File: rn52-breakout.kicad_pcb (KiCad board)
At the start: 2 copper layers, 15 parts, among them K1 CONN_3, P1 CONN_4, P2 CONN_2, P3 CONN_2, P4 CONN_2, U1 LM317T, U2 RN52

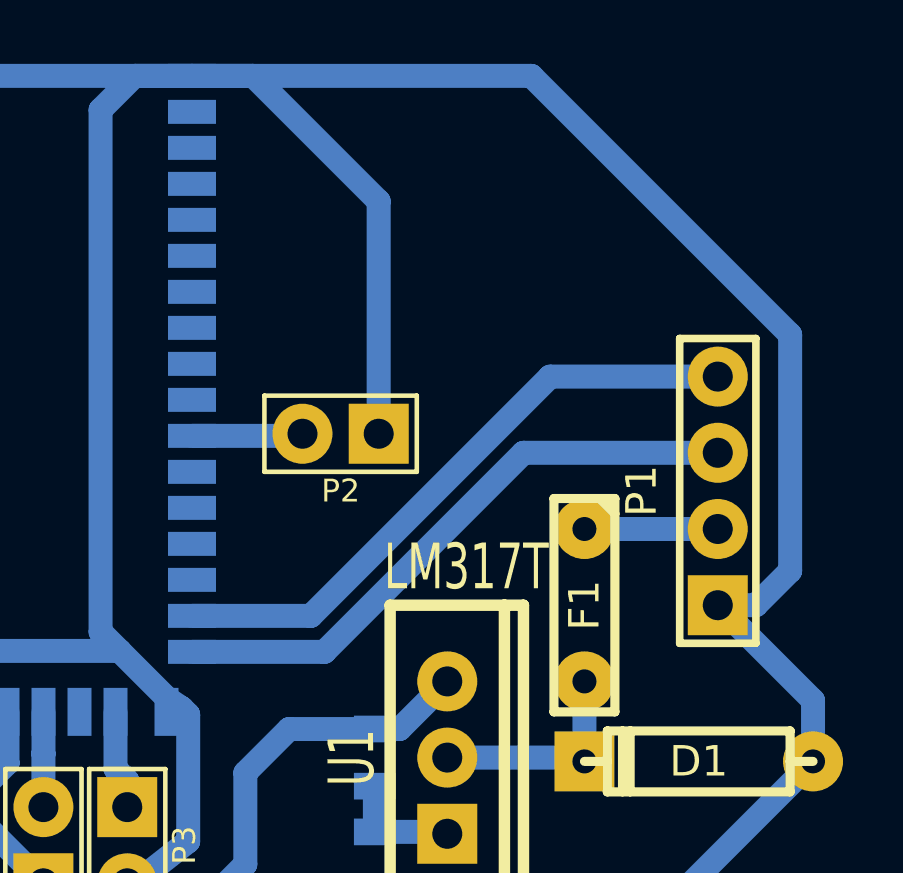
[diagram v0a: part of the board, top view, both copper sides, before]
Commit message: Pre-production version, still need a footprint for audio connector
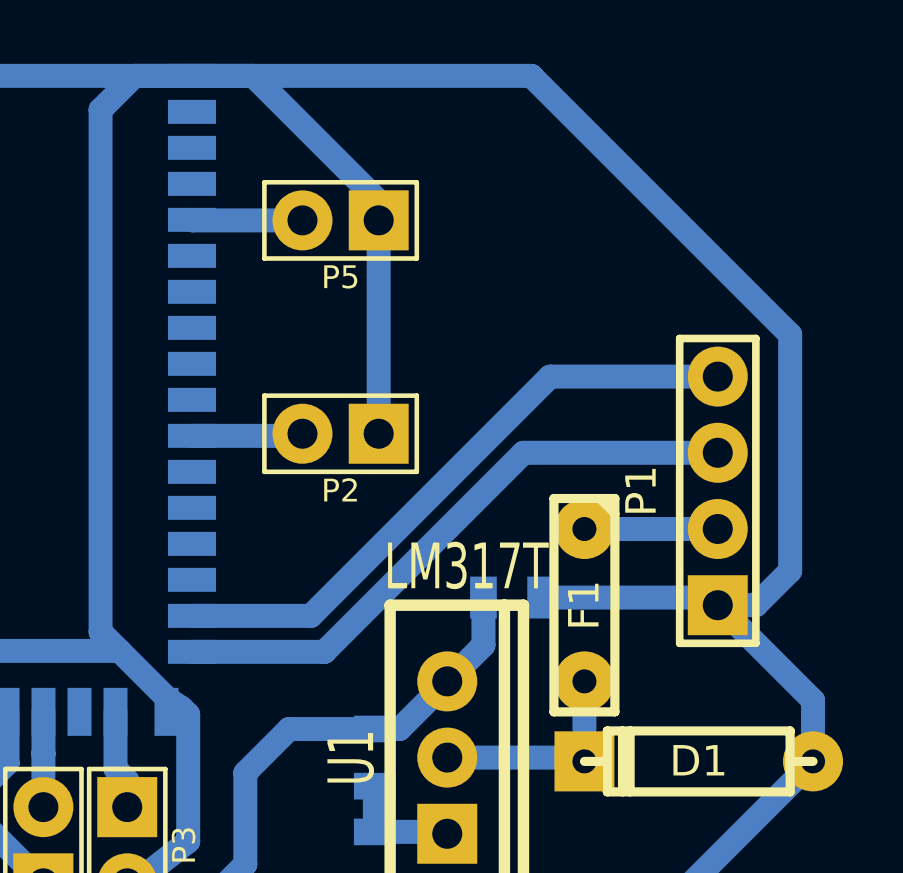
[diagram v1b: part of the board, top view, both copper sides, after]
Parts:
- added C1: 1uF, SM0805, B.Cu at (70.2, 35.8)
- added P5: FACTORY, PIN_ARRAY_2X1, F.Cu at (64.5, 23.2)
- P1: value CONN_4 -> UART
- P2: value CONN_2 -> MODE_SET
- P3: value CONN_2 -> BAUD_SET
- P4: value CONN_2 -> PWREN
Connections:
- U2 pad 5: (no net) -> N-0000011
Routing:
- net GND: track 129.5 -> 135.5 mm
- net N-0000011: track 0.00 -> 3.69 mm
- net +3.3V: track 49.6 -> 52.9 mm

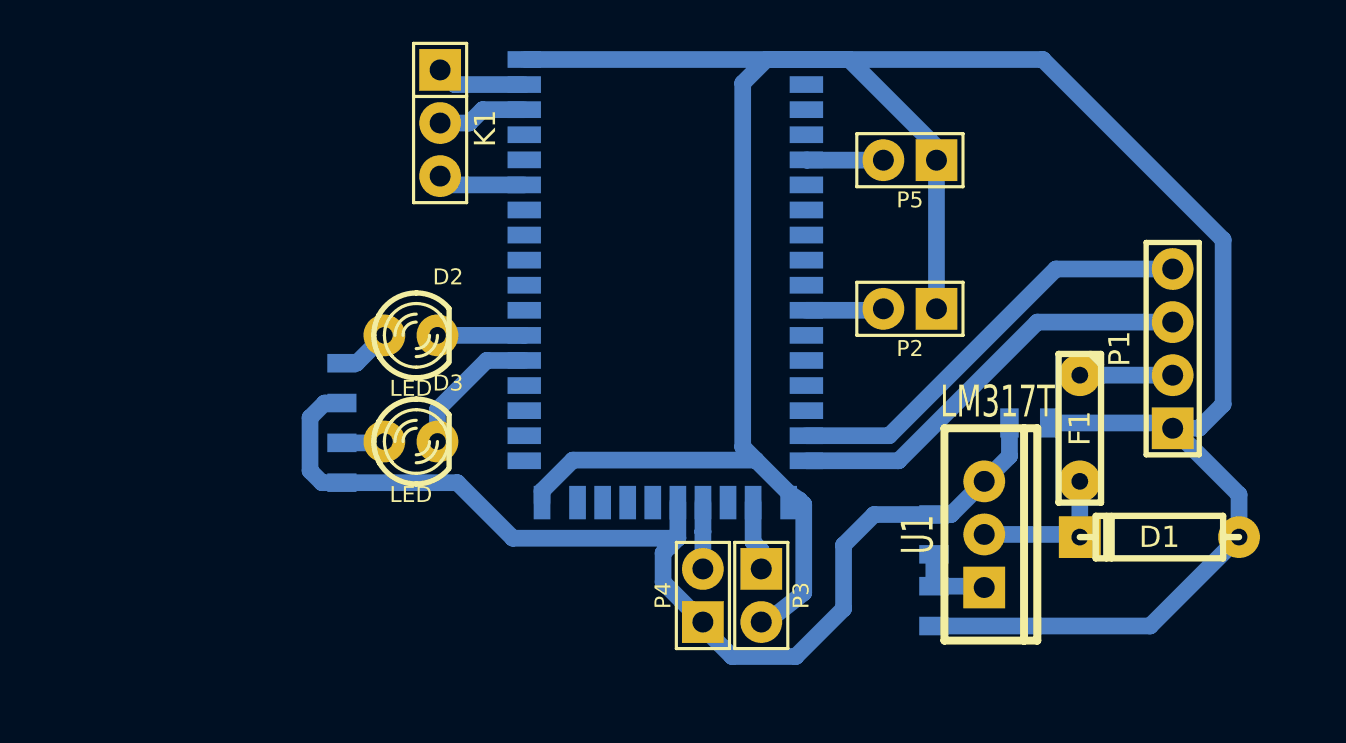
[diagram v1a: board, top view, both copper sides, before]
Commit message: Added 3.5mm jack connector
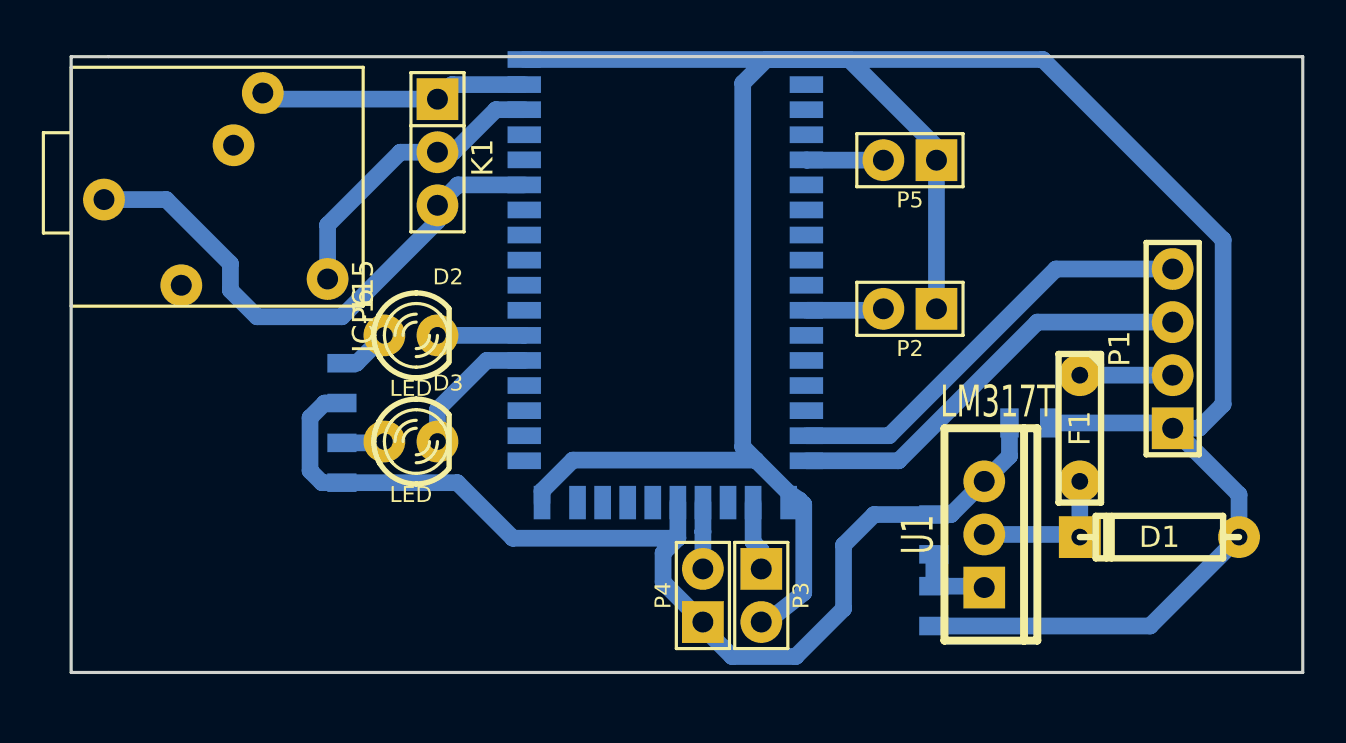
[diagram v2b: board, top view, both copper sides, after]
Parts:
- added P6: JC-115, JC-115, F.Cu at (38.4, 30.2)
- moved K1 1.40 mm to (41.9, 22.9)
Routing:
- net N-0000010: track 4.20 -> 26.2 mm
- net N-0000011: track 4.29 -> 14.3 mm
- net N-0000012: track 4.32 -> 12.9 mm
- added copper zone on B.Cu, net GND
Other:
- board outline added: 58.9 x 29.5 mm

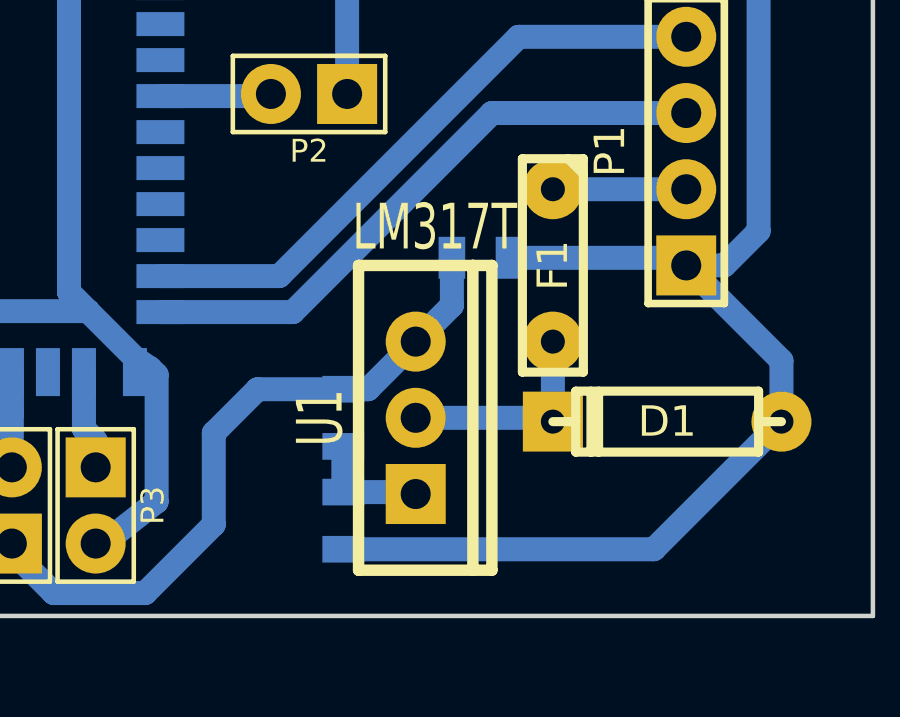
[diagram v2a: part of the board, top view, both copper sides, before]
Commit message: Fixed incorrect pinout for lin. regul., added some vanity pictures
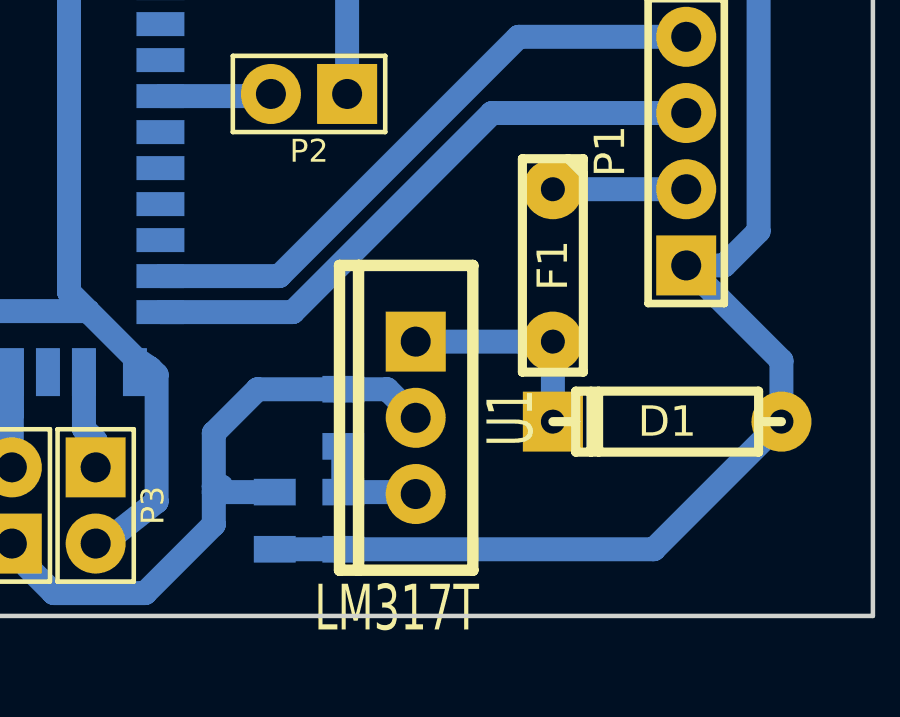
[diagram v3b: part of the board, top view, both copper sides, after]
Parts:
- moved C1 11.1 mm to (63.4, 44.6), turned to 270 degrees
- turned U1 to 180 degrees
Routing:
- net GND: track 135.5 -> 131.7 mm
- net +3.3V: track 52.9 -> 52.0 mm
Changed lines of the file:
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@@
     (thickness 1.6)
     (drawings 8)
-    (tracks 103)
+    (tracks 104)
     (zones 0)
     (modules 18)
@@
   )
   (module TO220_VERT (layer F.Cu)
-    (at 68.072 41.148)
+    (at 68.072 41.148 180)
     (descr "Regulateur TO220 serie LM78xx")
     (tags "TR TO220")
-    (fp_text reference U1 (at -3.175 0 90) (layer F.SilkS)
+    (fp_text reference U1 (at -3.175 0 270) (layer F.SilkS)
       (effects (font (size 1.524 1.016) (thickness 0.2032)))
     )
-    (fp_text value LM317T (at 0.635 -6.35) (layer F.SilkS)
+    (fp_text value LM317T (at 0.635 -6.35 180) (layer F.SilkS)
       (effects (font (size 1.524 1.016) (thickness 0.2032)))
     )
@@
     (fp_line (start 1.905 5.08) (end -1.905 5.08) (layer F.SilkS) (width 0.381))
     (fp_line (start -1.905 5.08) (end -1.905 -5.08) (layer F.SilkS) (width 0.381))
-    (pad 2 thru_hole circle (at 0 -2.54) (size 2 2) (drill 1)
+    (pad 1 thru_hole circle (at 0 -2.54 180) (size 2 2) (drill 1)
+      (layers *.Cu *.Mask F.SilkS)
+      (net 15 N-000005)
+    )
+    (pad 2 thru_hole circle (at 0 0 180) (size 2 2) (drill 1)
       (layers *.Cu *.Mask F.SilkS)
       (net 1 +3.3V)
     )
-    (pad 3 thru_hole circle (at 0 0) (size 2 2) (drill 1)
+    (pad 3 thru_hole rect (at 0 2.54 180) (size 2 2) (drill 1)
       (layers *.Cu *.Mask F.SilkS)
       (net 18 N-000006)
     )
-    (pad 1 thru_hole rect (at 0 2.54) (size 2 2) (drill 1)
-      (layers *.Cu *.Mask F.SilkS)
-      (net 15 N-000005)
-    )
   )
   (module SM0805 (layer B.Cu)
-    (at 70.231 35.814)
+    (at 63.373 44.577 270)
     (attr smd)
-    (fp_text reference C1 (at 0 0.3175) (layer B.SilkS)
+    (fp_text reference C1 (at 0 0.3175 270) (layer B.SilkS)
       (effects (font (size 0.50038 0.50038) (thickness 0.10922)) (justify mirror))
     )
-    (fp_text value 1uF (at 0 -0.381) (layer B.SilkS)
+    (fp_text value 1uF (at 0 -0.381 270) (layer B.SilkS)
       (effects (font (size 0.50038 0.50038) (thickness 0.10922)) (justify mirror))
     )
@@
     (fp_line (start 1.524 0.762) (end 1.524 -0.762) (layer B.SilkS) (width 0.09906))
     (fp_line (start 1.524 -0.762) (end 0.508 -0.762) (layer B.SilkS) (width 0.09906))
-    (pad 1 smd rect (at -0.9525 0) (size 0.889 1.397)
+    (pad 1 smd rect (at -0.9525 0 270) (size 0.889 1.397)
       (layers B.Cu B.Paste B.Mask)
       (net 1 +3.3V)
     )
-    (pad 2 smd rect (at 0.9525 0) (size 0.889 1.397)
+    (pad 2 smd rect (at 0.9525 0 270) (size 0.889 1.397)
       (layers B.Cu B.Paste B.Mask)
       (net 3 GND)
@@
   (gr_line (start 26.162 47.752) (end 83.312 47.752) (angle 90) (layer Edge.Cuts) (width 0.15))
   (gr_line (start 83.312 18.288) (end 83.312 47.752) (angle 90) (layer Edge.Cuts) (width 0.15))
-  (segment (start 69.2785 35.814) (end 69.2785 37.4015) (width 0.8) (layer B.Cu) (net 1))
-  (segment (start 69.2785 37.4015) (end 68.072 38.608) (width 0.8) (layer B.Cu) (net 1))
+  (segment (start 63.373 43.6245) (end 61.341 43.6245) (width 0.8) (layer B.Cu) (net 1))
+  (segment (start 61.595 43.434) (end 61.341 43.434) (width 0.8) (layer B.Cu) (net 1))
+  (segment (start 61.5315 43.434) (end 61.595 43.434) (width 0.8) (layer B.Cu) (net 1))
+  (segment (start 61.341 43.6245) (end 61.5315 43.434) (width 0.8) (layer B.Cu) (net 1))
+  (segment (start 65.659 40.1955) (end 67.1195 40.1955) (width 0.8) (layer B.Cu) (net 1))
+  (segment (start 67.1195 40.1955) (end 68.072 41.148) (width 0.8) (layer B.Cu) (net 1))
   (segment (start 54.61 45.339) (end 54.61 45.593) (width 0.8) (layer B.Cu) (net 1))
   (segment (start 62.8015 40.1955) (end 65.659 40.1955) (width 0.8) (layer B.Cu) (net 1))
   (segment (start 61.341 41.656) (end 62.8015 40.1955) (width 0.8) (layer B.Cu) (net 1))
-  (segment (start 61.341 44.704) (end 61.341 41.656) (width 0.8) (layer B.Cu) (net 1))
+  (segment (start 61.341 44.704) (end 61.341 43.434) (width 0.8) (layer B.Cu) (net 1))
+  (segment (start 61.341 43.434) (end 61.341 41.656) (width 0.8) (layer B.Cu) (net 1))
   (segment (start 59.055 46.99) (end 61.341 44.704) (width 0.8) (layer B.Cu) (net 1))
   (segment (start 56.007 46.99) (end 59.055 46.99) (width 0.8) (layer B.Cu) (net 1))
@@
   (segment (start 45.52 41.329) (end 53.413 41.329) (width 0.8) (layer B.Cu) (net 1))
   (segment (start 42.8625 38.6715) (end 45.52 41.329) (width 0.8) (layer B.Cu) (net 1))
-  (segment (start 65.659 40.1955) (end 66.4845 40.1955) (width 0.8) (layer B.Cu) (net 1))
-  (segment (start 66.4845 40.1955) (end 68.072 38.608) (width 0.8) (layer B.Cu) (net 1))
   (segment (start 53.413 39.624) (end 53.413 41.329) (width 0.8) (layer B.Cu) (net 1))
   (segment (start 53.413 41.329) (end 52.705 42.037) (width 0.8) (layer B.Cu) (net 1))
@@
   (segment (start 36.5125 34.8615) (end 35.814 35.56) (width 0.8) (layer B.Cu) (net 1))
   (segment (start 77.089 33.528) (end 72.644 33.528) (width 0.8) (layer B.Cu) (net 2))
-  (segment (start 71.1835 35.814) (end 76.835 35.814) (width 0.8) (layer B.Cu) (net 3))
-  (segment (start 76.835 35.814) (end 77.089 36.068) (width 0.8) (layer B.Cu) (net 3))
+  (segment (start 63.373 45.5295) (end 65.659 45.5295) (width 0.8) (layer B.Cu) (net 3))
   (segment (start 46.063 18.424) (end 59.563 18.424) (width 0.8) (layer B.Cu) (net 3))
   (segment (start 77.089 36.068) (end 78.359 36.068) (width 0.8) (layer B.Cu) (net 3))
@@
   (segment (start 59.436 43.942) (end 59.436 39.712) (width 0.8) (layer B.Cu) (net 3))
   (segment (start 57.658 45.339) (end 59.436 43.942) (width 0.8) (layer B.Cu) (net 3))
-  (segment (start 41.91 25.4) (end 41.91 26.162) (width 0.8) (layer B.Cu) (net 4) (status C00000))
-  (segment (start 28.936 25.126) (end 25.954 25.126) (width 0.8) (layer B.Cu) (net 4) (status 800000))
+  (segment (start 41.91 25.4) (end 41.91 26.162) (width 0.8) (layer B.Cu) (net 4))
+  (segment (start 28.936 25.126) (end 25.954 25.126) (width 0.8) (layer B.Cu) (net 4))
   (segment (start 32.004 28.194) (end 28.936 25.126) (width 0.8) (layer B.Cu) (net 4))
   (segment (start 32.004 29.464) (end 32.004 28.194) (width 0.8) (layer B.Cu) (net 4))
   (segment (start 33.274 30.734) (end 32.004 29.464) (width 0.8) (layer B.Cu) (net 4))
   (segment (start 37.338 30.734) (end 33.274 30.734) (width 0.8) (layer B.Cu) (net 4))
-  (segment (start 41.91 26.162) (end 37.338 30.734) (width 0.8) (layer B.Cu) (net 4) (status 400000))
+  (segment (start 41.91 26.162) (end 37.338 30.734) (width 0.8) (layer B.Cu) (net 4))
   (segment (start 46.063 24.424) (end 42.886 24.424) (width 0.8) (layer B.Cu) (net 4))
   (segment (start 42.886 24.424) (end 41.91 25.4) (width 0.8) (layer B.Cu) (net 4))
-  (segment (start 41.91 22.86) (end 40.132 22.86) (width 0.8) (layer B.Cu) (net 5) (status 400000))
-  (segment (start 36.654 26.338) (end 36.654 28.926) (width 0.8) (layer B.Cu) (net 5) (status 800000))
+  (segment (start 41.91 22.86) (end 40.132 22.86) (width 0.8) (layer B.Cu) (net 5))
+  (segment (start 36.654 26.338) (end 36.654 28.926) (width 0.8) (layer B.Cu) (net 5))
   (segment (start 40.132 22.86) (end 36.654 26.338) (width 0.8) (layer B.Cu) (net 5))
   (segment (start 46.063 20.824) (end 44.708 20.824) (width 0.8) (layer B.Cu) (net 5))
   (segment (start 42.672 22.86) (end 41.91 22.86) (width 0.8) (layer B.Cu) (net 5))
   (segment (start 44.708 20.824) (end 42.672 22.86) (width 0.8) (layer B.Cu) (net 5))
-  (segment (start 41.91 20.32) (end 33.848 20.32) (width 0.8) (layer B.Cu) (net 6) (status C00000))
-  (segment (start 33.848 20.32) (end 33.554 20.026) (width 0.8) (layer B.Cu) (net 6) (status C00000))
+  (segment (start 41.91 20.32) (end 33.848 20.32) (width 0.8) (layer B.Cu) (net 6))
+  (segment (start 33.848 20.32) (end 33.554 20.026) (width 0.8) (layer B.Cu) (net 6))
   (segment (start 46.063 19.624) (end 42.606 19.624) (width 0.8) (layer B.Cu) (net 6))
   (segment (start 42.606 19.624) (end 41.91 20.32) (width 0.8) (layer B.Cu) (net 6))
@@
   (segment (start 54.61 41.021) (end 54.613 41.018) (width 0.8) (layer B.Cu) (net 14))
   (segment (start 65.659 43.6245) (end 68.0085 43.6245) (width 0.8) (layer B.Cu) (net 15))
+  (segment (start 65.659 42.1005) (end 65.659 43.6245) (width 0.8) (layer B.Cu) (net 15))
   (segment (start 68.0085 43.6245) (end 68.072 43.688) (width 0.8) (layer B.Cu) (net 15))
-  (segment (start 65.659 42.1005) (end 65.659 43.6245) (width 0.8) (layer B.Cu) (net 15))
   (segment (start 37.338 32.9565) (end 38.0365 32.9565) (width 0.8) (layer B.Cu) (net 16))
   (segment (start 38.0365 32.9565) (end 39.37 31.623) (width 0.8) (layer B.Cu) (net 16))
@@
   (segment (start 70.612 30.988) (end 77.089 30.988) (width 0.8) (layer B.Cu) (net 17))
   (segment (start 63.976 37.624) (end 70.612 30.988) (width 0.8) (layer B.Cu) (net 17))
+  (segment (start 72.644 38.608) (end 68.072 38.608) (width 0.8) (layer B.Cu) (net 18))
   (segment (start 72.644 41.275) (end 72.644 38.608) (width 0.8) (layer B.Cu) (net 18))
-  (segment (start 68.453 41.148) (end 72.517 41.148) (width 0.8) (layer B.Cu) (net 18))
-  (segment (start 72.517 41.148) (end 72.644 41.275) (width 0.8) (layer B.Cu) (net 18))
   (zone (net 3) (net_name GND) (layer B.Cu) (hatch edge 0.508)
     (connect_pads (clearance 0.5))
